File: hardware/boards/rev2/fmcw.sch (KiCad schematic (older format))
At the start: 24 parts, among them U1 LP5907MFX-3.3, U2 LP5907MFX-1.8, U3 KT2520K-T, U4 NC7SVU04P5X, U5 NB3N551

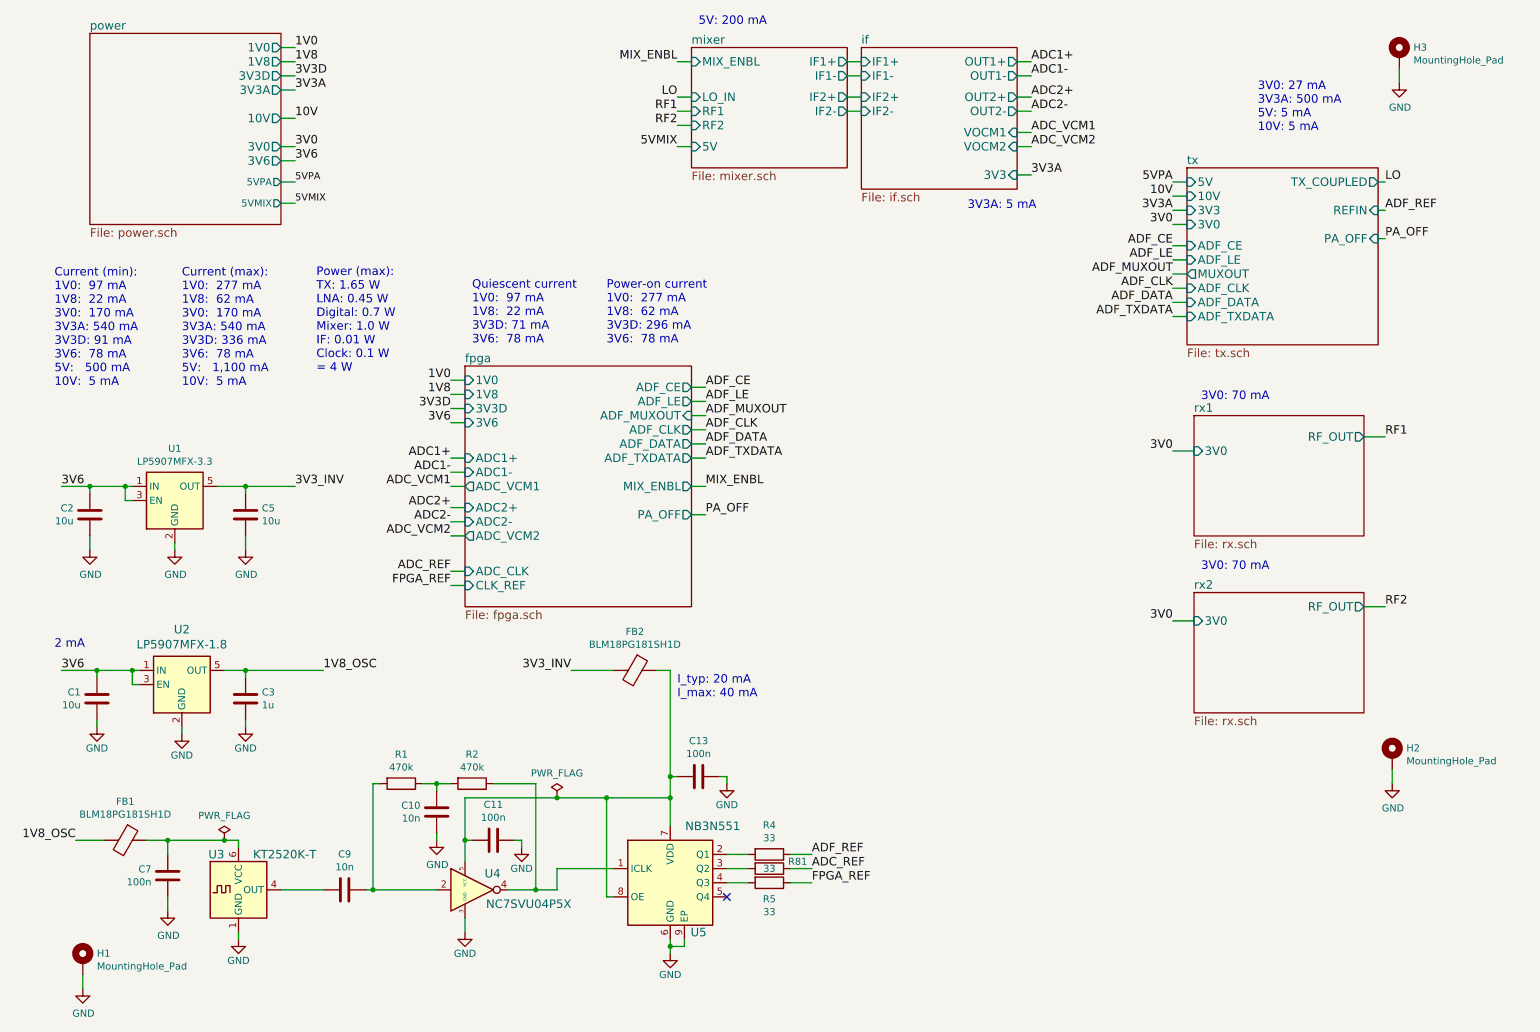
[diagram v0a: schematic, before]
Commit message: reorganize schematic
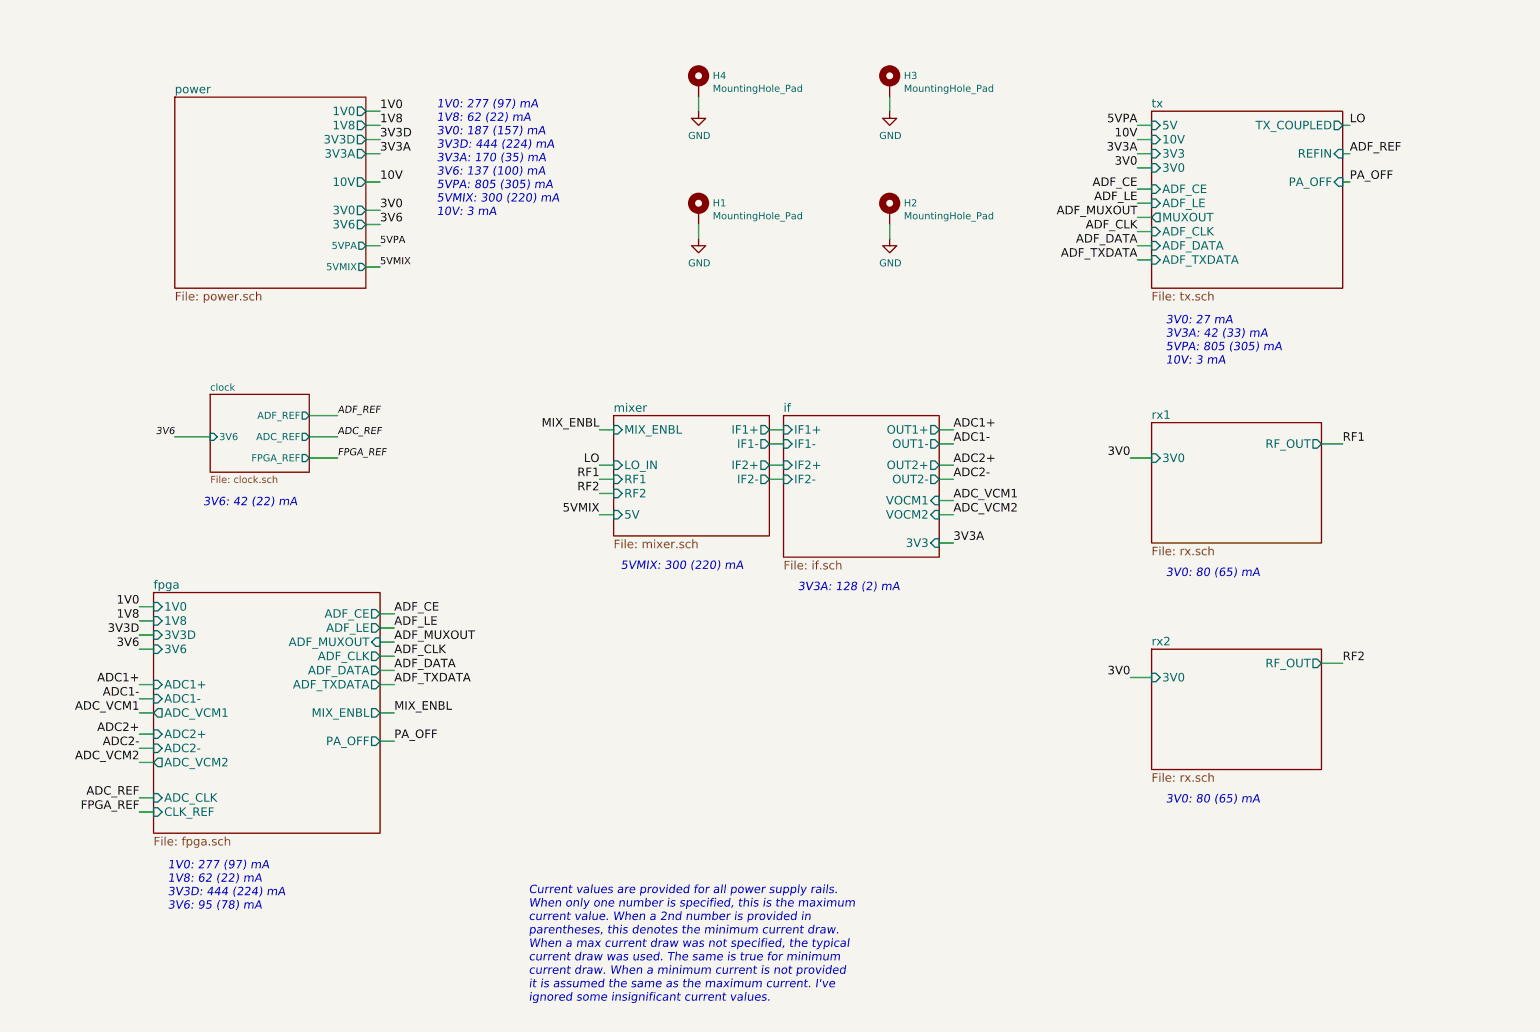
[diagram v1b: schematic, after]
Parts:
- removed C1, C2, C5: 10u, Capacitor_SMD:C_0805_2012Metric, symbol Device:C
- removed C10, C9: 10n, Capacitor_SMD:C_0402_1005Metric, symbol Device:C
- removed C11, C13, C7: 100n, Capacitor_SMD:C_0402_1005Metric, symbol Device:C
- removed C3: 1u, Capacitor_SMD:C_0805_2012Metric, symbol Device:C
- removed FB1, FB2: BLM18PG181SH1D, Inductor_SMD:L_0603_1608Metric, symbol Device:Ferrite_Bead
- removed R1, R2: 470k, Resistor_SMD:R_0402_1005Metric, symbol Device:R
- removed R4, R5, R81: 33, Resistor_SMD:R_0402_1005Metric, symbol Device:R
- removed U1: LP5907MFX-3.3, Package_TO_SOT_SMD:SOT-23-5, symbol Regulator_Linear:LP5907MFX-3.3
- removed U2: LP5907MFX-1.8, Package_TO_SOT_SMD:SOT-23-5, symbol Regulator_Linear:LP5907MFX-1.8
- removed U3: KT2520K-T, Oscillator:Oscillator_SMD_Kyocera_2520-6Pin_2.5x2.0mm, symbol Oscillator:KT2520K-T
- removed U4: NC7SVU04P5X, Package_TO_SOT_SMD:SOT-353_SC-70-5, symbol 74xGxx:NC7SVU04P5X
- removed U5: NB3N551, Package_DFN_QFN:DFN-8-1EP_2x2mm_P0.5mm_EP0.9x1.3mm, symbol Interface:NB3N551MN
- added H4: MountingHole_Pad, MountingHole:MountingHole_3.2mm_M3_Pad_Via, symbol Mechanical:MountingHole_Pad
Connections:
- net GND: now also H4.1
- no-connect marks 1 -> 0
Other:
- note added: "1V0: 277 (97) mA\n1V8: 62 (22) mA\n3V0: 187 (157) mA\n3V3D: 444 (224) mA\n3V3A: 170 (35) mA\n3V6: 137 (100) mA\n5VPA: 805 (305) mA\n5VMIX: 300 (220) mA\n10V: 3 mA"
- note added: "1V0: 277 (97) mA\n1V8: 62 (22) mA\n3V3D: 444 (224) mA\n3V6: 95 (78) mA"
- note added: "3V0: 27 mA\n3V3A: 42 (33) mA\n5VPA: 805 (305) mA\n10V: 3 mA"
- note added: "3V0: 80 (65) mA"
- note added: "3V3A: 128 (2) mA"
- note added: "3V6: 42 (22) mA"
- note added: "5VMIX: 300 (220) mA"
- note added: "Current values are provided for all power supply rails.\nWhen only one number is specified, this is the maximum\ncurrent value. When a 2nd number is provided in\nparentheses, this denotes the minimum current draw.\nWhen a max current draw was not specified, the typical\ncurrent draw was used. The same is true for minimum\ncurrent draw. When a minimum current is not provided\nit is assumed the sam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"
- note removed: "2 mA"
- note removed: "3V0: 27 mA\n3V3A: 500 mA\n5V: 5 mA\n10V: 5 mA"
- note removed: "3V0: 70 mA"
- note removed: "3V3A: 5 mA"
- note removed: "5V: 200 mA"
- note removed: "Current (max):\n1V0: 277 mA\n1V8: 62 mA\n3V0: 170 mA\n3V3A: 540 mA\n3V3D: 336 mA\n3V6: 78 mA\n5V: 1,100 mA\n10V: 5 mA"
- note removed: "Current (min):\n1V0: 97 mA\n1V8: 22 mA\n3V0: 170 mA\n3V3A: 540 mA\n3V3D: 91 mA\n3V6: 78 mA\n5V: 500 mA\n10V: 5 mA"
- note removed: "I_typ: 20 mA\nI_max: 40 mA"
- note removed: "Power (max):\nTX: 1.65 W\nLNA: 0.45 W\nDigital: 0.7 W\nMixer: 1.0 W\nIF: 0.01 W\nClock: 0.1 W\n= 4 W"
- note removed: "Power-on current\n1V0: 277 mA\n1V8: 62 mA\n3V3D: 296 mA\n3V6: 78 mA"
- note removed: "Quiescent current\n1V0: 97 mA\n1V8: 22 mA\n3V3D: 71 mA\n3V6: 78 mA"
- moved on the sheet: H1, H2, H3

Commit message: revert to kicad v5 for pcb gen
V6 contains a few bugs and a V6 board cannot be edited with V5.
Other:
- note added: "1V0: 277 (97) mA\n1V8: 62 (22) mA\n3V0: 187 (157) mA\n3V3D: 444 (224) mA\n3V3A: 118 (35) mA\n3V6: 137 (100) mA\n5VPA: 805 (305) mA\n5VMIX: 300 (220) mA\n10V: 3 mA"
- note added: "3V3A: 76 (2) mA"
- note added: "Note on track widths:\nThe OshPark min track width of 0.127mm is sufficient\nfor currents up to 165mA on internal and external\nlayers (internal layers require wider traces for the same \ncurrent capacity). It is therefore used for all signal traces.\nExternal layers do not need to use trace widths larger\nthan 0.3mm for any power rail. This includes ground\nconnections as well. For internal laye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"
- note removed: "1V0: 277 (97) mA\n1V8: 62 (22) mA\n3V0: 187 (157) mA\n3V3D: 444 (224) mA\n3V3A: 170 (35) mA\n3V6: 137 (100) mA\n5VPA: 805 (305) mA\n5VMIX: 300 (220) mA\n10V: 3 mA"
- note removed: "3V3A: 128 (2) mA"
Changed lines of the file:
@@
-EESchema Schematic File Version 5
-EELAYER 33 0
+EESchema Schematic File Version 4
+EELAYER 30 0
 EELAYER END
 $Descr A4 11693 8268
@@
 Comment3 ""
 Comment4 ""
-Comment5 ""
-Comment6 ""
-Comment7 ""
-Comment8 ""
-Comment9 ""
 $EndDescr
 Wire Wire Line
@@
 	3200 5600 3100 5600
 Wire Wire Line
-	4650 3850 4750 3850
-Wire Wire Line
-	4650 4200 4750 4200
-Wire Wire Line
-	4750 3600 4650 3600
-Wire Wire Line
-	4750 3950 4650 3950
-Wire Wire Line
-	4750 4050 4650 4050
+	4650 3150 4750 3150
+Wire Wire Line
+	4650 3500 4750 3500
+Wire Wire Line
+	4750 2900 4650 2900
+Wire Wire Line
+	4750 3250 4650 3250
+Wire Wire Line
+	4750 3350 4650 3350
 Wire Wire Line
 	5350 1350 5350 1250
@@
 	5350 2250 5350 2150
 Wire Wire Line
-	5850 3600 5950 3600
-Wire Wire Line
-	5850 3700 5950 3700
-Wire Wire Line
-	5850 3850 5950 3850
-Wire Wire Line
-	5850 3950 5950 3950
+	5850 2900 5950 2900
+Wire Wire Line
+	5850 3000 5950 3000
+Wire Wire Line
+	5850 3150 5950 3150
+Wire Wire Line
+	5850 3250 5950 3250
 Wire Wire Line
 	6700 1350 6700 1250
@@
 	6700 2250 6700 2150
 Wire Wire Line
-	7050 4100 7150 4100
-Wire Wire Line
-	7150 3600 7050 3600
+	7050 3400 7150 3400
+Wire Wire Line
+	7150 2900 7050 2900
+Wire Wire Line
+	7150 3000 7050 3000
+Wire Wire Line
+	7150 3150 7050 3150
+Wire Wire Line
+	7150 3250 7050 3250
+Wire Wire Line
+	7150 3500 7050 3500
 Wire Wire Line
 	7150 3700 7050 3700
-Wire Wire Line
-	7150 3850 7050 3850
-Wire Wire Line
-	7150 3950 7050 3950
-Wire Wire Line
-	7150 4200 7050 4200
-Wire Wire Line
-	7150 4400 7050 4400
 Wire Wire Line
 	8400 3800 8550 3800
@@
 3V6: 42 (22) mA
 Text Notes 3500 2100 0    59   Italic 0
-1V0: 277 (97) mA\n1V8: 62 (22) mA\n3V0: 187 (157) mA\n3V3D: 444 (224) mA\n3V3A: 170 (35) mA\n3V6: 137 (100) mA\n5VPA: 805 (305) mA\n5VMIX: 300 (220) mA\n10V: 3 mA
+1V0: 277 (97) mA\n1V8: 62 (22) mA\n3V0: 187 (157) mA\n3V3D: 444 (224) mA\n3V3A: 118 (35) mA\n3V6: 137 (100) mA\n5VPA: 805 (305) mA\n5VMIX: 300 (220) mA\n10V: 3 mA
+Text Notes 4150 6600 0    59   Italic 0
+Note on track widths:\nThe OshPark min track width of 0.127mm is sufficient\nfor currents up to 165mA on internal and external\nlayers (internal layers require wider traces for the same \ncurrent capacity). It is therefore used for all signal traces.\nExternal layers do not need to use trace widths larger\nthan 0.3mm for any power rail. This includes ground\nconnections as well. For internal layers, a trace width of\nat least 0.3mm (I<300mA) is used for all power rails\neven when they require less current. Current values\nbetween 300 and 500mA use a trace width of 0.6mm.\nValues between 500 and 1,000mA use a trace width of\n1.5mm and currents up to 1.5A use 2.7mm. Unfortunately,\nKiCAD does not yet support advanced constraints which\nwould make this process simpler. 50ohm characteristic\nimpedance traces are all routed on the top layer and use\na width of 0.38mm. 50ohm differential characteristic\nimpedance traces use a 0.85mm width. The minimum\nOshPark via drill diameter of 0.254mm should be\nsufficient for currents up to 1.7A and is therefore used\nfor all vias. All traces use the minimum trace clearance\nof 0.127mm except microstrips, which use a 0.8mm\nclearance.
 Text Notes 4150 7650 0    59   Italic 0
 Current values are provided for all power supply rails.\nWhen only one number is specified, this is the maximum\ncurrent value. When a 2nd number is provided in\nparentheses, this denotes the minimum current draw.\nWhen a max current draw was not specified, the typical\ncurrent draw was used. The same is true for minimum\ncurrent draw. When a minimum current is not provided\nit is assumed the same as the maximum current. I've\nignored some insignificant current values.
-Text Notes 4800 4600 0    59   Italic 0
+Text Notes 4800 3900 0    59   Italic 0
 5VMIX: 300 (220) mA
-Text Notes 6050 4750 0    59   Italic 0
-3V3A: 128 (2) mA
+Text Notes 6050 4050 0    59   Italic 0
+3V3A: 76 (2) mA
 Text Notes 8650 3150 0    59   Italic 0
 3V0: 27 mA\n3V3A: 42 (33) mA\n5VPA: 805 (305) mA\n10V: 3 mA
@@
 Text Label 3200 5800 0    60   ~ 0
 PA_OFF
-Text Label 4650 3600 2    60   ~ 0
+Text Label 4650 2900 2    60   ~ 0
 MIX_ENBL
-Text Label 4650 3850 2    60   ~ 0
+Text Label 4650 3150 2    60   ~ 0
 LO
-Text Label 4650 3950 2    60   ~ 0
+Text Label 4650 3250 2    60   ~ 0
 RF1
-Text Label 4650 4050 2    60   ~ 0
+Text Label 4650 3350 2    60   ~ 0
 RF2
-Text Label 4650 4200 2    60   ~ 0
+Text Label 4650 3500 2    60   ~ 0
 5VMIX
-Text Label 7150 3600 0    60   ~ 0
+Text Label 7150 2900 0    60   ~ 0
 ADC1+
+Text Label 7150 3000 0    60   ~ 0
+ADC1-
+Text Label 7150 3150 0    60   ~ 0
+ADC2+
+Text Label 7150 3250 0    60   ~ 0
+ADC2-
+Text Label 7150 3400 0    60   ~ 0
+ADC_VCM1
+Text Label 7150 3500 0    60   ~ 0
+ADC_VCM2
 Text Label 7150 3700 0    60   ~ 0
-ADC1-
-Text Label 7150 3850 0    60   ~ 0
-ADC2+
-Text Label 7150 3950 0    60   ~ 0
-ADC2-
-Text Label 7150 4100 0    60   ~ 0
-ADC_VCM1
-Text Label 7150 4200 0    60   ~ 0
-ADC_VCM2
-Text Label 7150 4400 0    60   ~ 0
 3V3A
 Text Label 8400 3800 2    60   ~ 0
@@
 $EndSheet
 $Sheet
-S 5950 3500 1100 1000
+S 5950 2800 1100 1000
 U 59665702
 F0 "if" 60
 F1 "if.sch" 60
-F2 "IF1+" I L 5950 3600 60
-F3 "IF1-" I L 5950 3700 60
-F4 "IF2+" I L 5950 3850 60
-F5 "IF2-" I L 5950 3950 60
-F6 "3V3" I R 7050 4400 60
-F7 "OUT1+" O R 7050 3600 60
-F8 "OUT1-" O R 7050 3700 60
-F9 "OUT2+" O R 7050 3850 60
-F10 "OUT2-" O R 7050 3950 60
-F11 "VOCM1" I R 7050 4100 60
-F12 "VOCM2" I R 7050 4200 60
+F2 "IF1+" I L 5950 2900 60
+F3 "IF1-" I L 5950 3000 60
+F4 "IF2+" I L 5950 3150 60
+F5 "IF2-" I L 5950 3250 60
+F6 "3V3" I R 7050 3700 60
+F7 "OUT1+" O R 7050 2900 60
+F8 "OUT1-" O R 7050 3000 60
+F9 "OUT2+" O R 7050 3150 60
+F10 "OUT2-" O R 7050 3250 60
+F11 "VOCM1" I R 7050 3400 60
+F12 "VOCM2" I R 7050 3500 60
 $EndSheet
 $Sheet
-S 4750 3500 1100 850
+S 4750 2800 1100 850
 U 59434BD2
 F0 "mixer" 60
 F1 "mixer.sch" 60
-F2 "MIX_ENBL" I L 4750 3600 60
-F3 "LO_IN" I L 4750 3850 60
-F4 "5V" I L 4750 4200 60
-F5 "IF1+" O R 5850 3600 60
-F6 "IF1-" O R 5850 3700 60
-F7 "RF1" I L 4750 3950 60
-F8 "RF2" I L 4750 4050 60
-F9 "IF2+" O R 5850 3850 60
-F10 "IF2-" O R 5850 3950 60
+F2 "MIX_ENBL" I L 4750 2900 60
+F3 "LO_IN" I L 4750 3150 60
+F4 "5V" I L 4750 3500 60
+F5 "IF1+" O R 5850 2900 60
+F6 "IF1-" O R 5850 3000 60
+F7 "RF1" I L 4750 3250 60
+F8 "RF2" I L 4750 3350 60
+F9 "IF2+" O R 5850 3150 60
+F10 "IF2-" O R 5850 3250 60
 $EndSheet
 $Sheet
